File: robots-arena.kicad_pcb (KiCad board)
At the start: 2 copper layers, 86.4 x 54.6 mm, 75 parts, among them J1 SMA, P1 CONN_PWM, P10 CONN_PWM, P11 CONN_01X09, P12 CONN_02X02, P13 JST_2, P14 CONN_02X07, P2 CONN_PWM, P3 CONN_PWM, P4 CONN_PWM, P5 CONN_PWM, P6 CONN_PWM, P7 CONN_PWM, P8 CONN_23X2, P9 CONN_23X2, SW1 DIPSW_02, SW2 SW_PUSH, U1 MPU-9150, U2 CAT24C256W, U3 MTK339, U4 XBee_Header, U5 LPS331AP

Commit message: Layout completed
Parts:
- moved G*** 54.3 mm to (165.9, 98.0)
- moved JP2 3.30 mm to (127.0, 110.0)
- moved JP3 3.30 mm to (129.5, 110.0)
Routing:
- net DGND: track 50.6 -> 424.8 mm, vias 1 -> 25
- net 3V3: track 22.2 -> 230.9 mm, vias 0 -> 11
- net I2C_2_SDA: track 0.35 -> 75.6 mm, vias 0 -> 3
- net I2C_2_SCL: track 0.00 -> 74.4 mm, vias 0 -> 2
- net BEE_DTR: track 0.00 -> 43.6 mm
- net UART_5_RTS: track 16.0 -> 55.4 mm, vias 0 -> 1
- net Net-(BT1-Pad1): track 0.00 -> 36.2 mm, vias 0 -> 1
- net UART_5_CTS: track 5.78 -> 41.6 mm
- net UART_5_RX: track 0.00 -> 35.8 mm, vias 0 -> 1
- net INT_M: track 0.00 -> 35.6 mm, vias 0 -> 2
- net +5V: track 20.3 -> 54.9 mm
- net UART_5_TX: track 0.00 -> 32.2 mm, vias 0 -> 1
- net ADC_IN_1: track 0.00 -> 28.9 mm
- net UART_1_TX: track 0.00 -> 28.7 mm
- net ADC_IN_0: track 0.00 -> 28.7 mm
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- added copper zone on F.Cu, net DGND
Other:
- board text added: "1 0 3 2 5 4 6"
- board text added: "1 2 3 4 5 6 7 8"
- board text added: "ADC"
- board text added: "Bee Header"
- board text added: "GPS"
- board text added: "IMU"
- board text added: "PWM"
- board text added: "Robot Arena cape v2 Salaheddine Missri EPFL - LA"

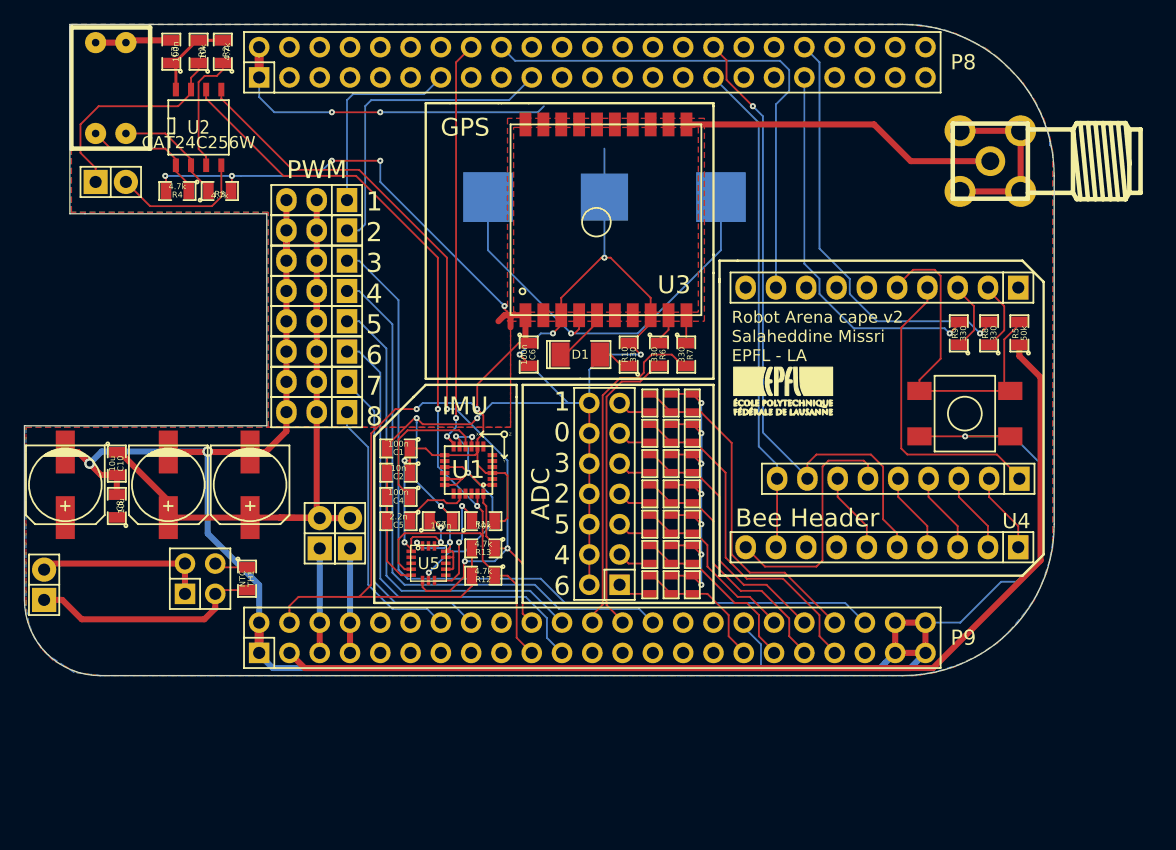
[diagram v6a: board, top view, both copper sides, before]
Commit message: Correct XBee header & Update layout and Gerber files
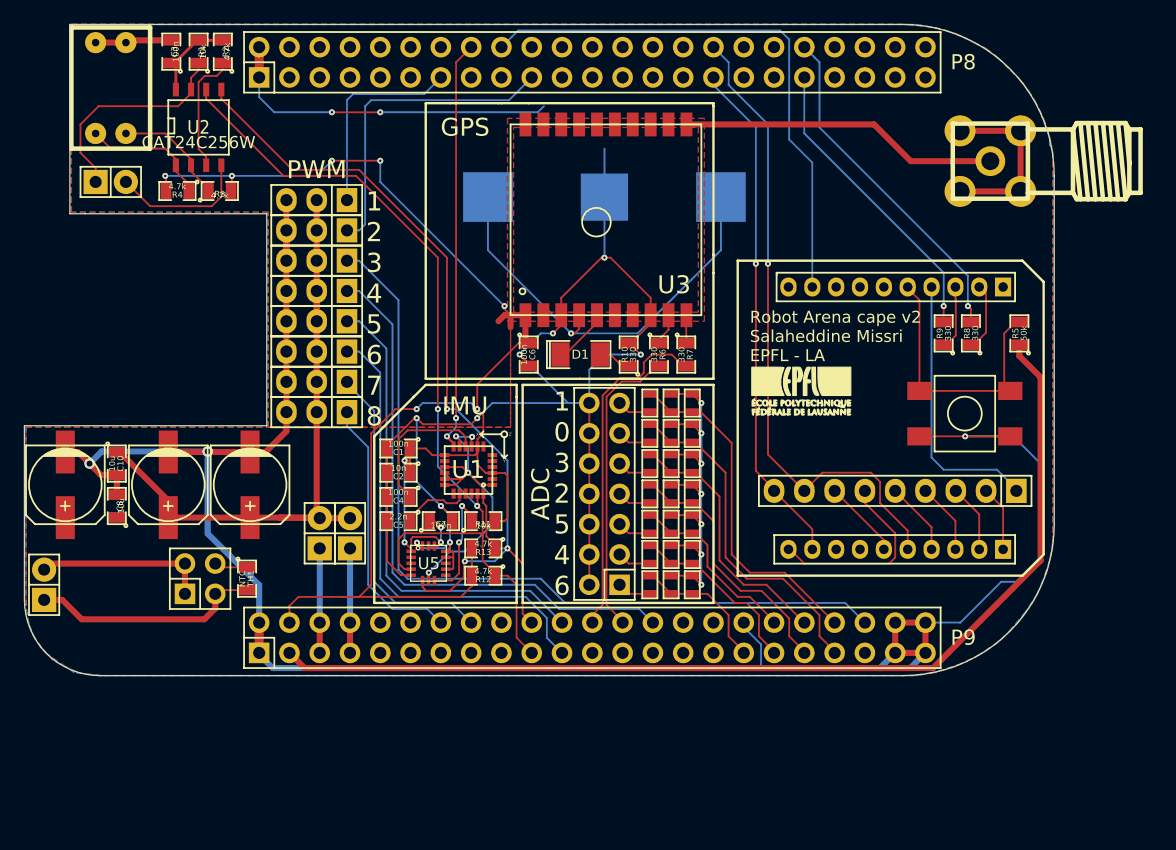
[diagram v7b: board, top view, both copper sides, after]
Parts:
- moved G*** 1.52 mm to (167.4, 98.0)
- moved R8 1.52 mm to (181.6, 93.2)
- moved U4 1.30 mm to (175.5, 100.3)
- moved R9 1.27 mm to (179.3, 93.2)
- moved P11 1.05 mm to (175.3, 106.4)
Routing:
- net UART_5_RX: track 35.8 -> 28.8 mm
- net UART_5_TX: track 32.2 -> 25.4 mm
- net Net-(R5-Pad2): track 29.1 -> 23.4 mm
- net Net-(P11-Pad6): track 20.5 -> 16.3 mm
- net BEE_DTR: track 43.6 -> 46.8 mm
- net Net-(P11-Pad1): track 25.4 -> 22.7 mm
- net UART_5_CTS: track 41.6 -> 43.0 mm, vias 0 -> 1
- net Net-(P11-Pad2): track 6.76 -> 5.50 mm
- net Net-(P11-Pad3): track 6.76 -> 5.72 mm
- net Net-(P11-Pad4): track 6.76 -> 5.94 mm
- net Net-(P11-Pad5): track 6.76 -> 6.17 mm
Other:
- board text removed: "Bee Header"
